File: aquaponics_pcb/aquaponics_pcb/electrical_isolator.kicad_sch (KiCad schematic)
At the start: 0 parts

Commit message: update isolator circuit
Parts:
- added C10: 1uF, Capacitor_SMD:C_0603_1608Metric_Pad1.08x0.95mm_HandSolder, symbol Device:C
- added C11: 100nF, Capacitor_SMD:C_0603_1608Metric_Pad1.08x0.95mm_HandSolder, symbol Device:C
- added C9: 10uF, Capacitor_SMD:C_0603_1608Metric_Pad1.08x0.95mm_HandSolder, symbol Device:C
- added IC3: ADM3260ARSZ, SOP65P780X200-20N, symbol SamacSys_Parts:ADM3260ARSZ
- added Q2: SSM6N35AFE,LF, SOTFL50P160X60-6N, symbol SamacSys_Parts:SSM6N35AFE,LF
- added R11, R12: 1M, Resistor_SMD:R_0603_1608Metric_Pad0.98x0.95mm_HandSolder, symbol Device:R_US
- added R13: 10k, Resistor_SMD:R_0603_1608Metric_Pad0.98x0.95mm_HandSolder, symbol Device:R_US
- added R14, R15, R16: 4.7k, Resistor_SMD:R_0603_1608Metric_Pad0.98x0.95mm_HandSolder, symbol Device:R_US
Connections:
- new net: IC3.13 (VSEL), R13.2, R14.1
- new net: IC3.8 (PDIS), Q2.6 (D), R11.2
- new net Earth_Clean: IC3.11 (GNDISO_1), IC3.14 (GNDISO_2), IC3.16 (GNDISO_3), IC3.20 (GNDISO_4), R14.2
- new net GND: C10.2, C11.2, C9.2, IC3.1 (GNDP_1), IC3.10 (GNDP_4), IC3.5 (GNDP_2), IC3.7 (GNDP_3), Q2.1 (S)
- new net ISO_EN: Q2.2 (G), R12.2
- new net ISO_SCL: IC3.19 (SCL1), R15.2
- new net ISO_SDA: IC3.18 (SDA1), R16.2
- new net SCL: IC3.2 (SCL2)
- new net SDA: IC3.3 (SDA2)
- new net VIN: C10.1, C11.1, C9.1, IC3.4 (VDDP), IC3.9 (VIN), R11.1, R12.1
- new net VISO: IC3.12 (VISO), IC3.17 (VDDISO), R13.1, R15.1, R16.1

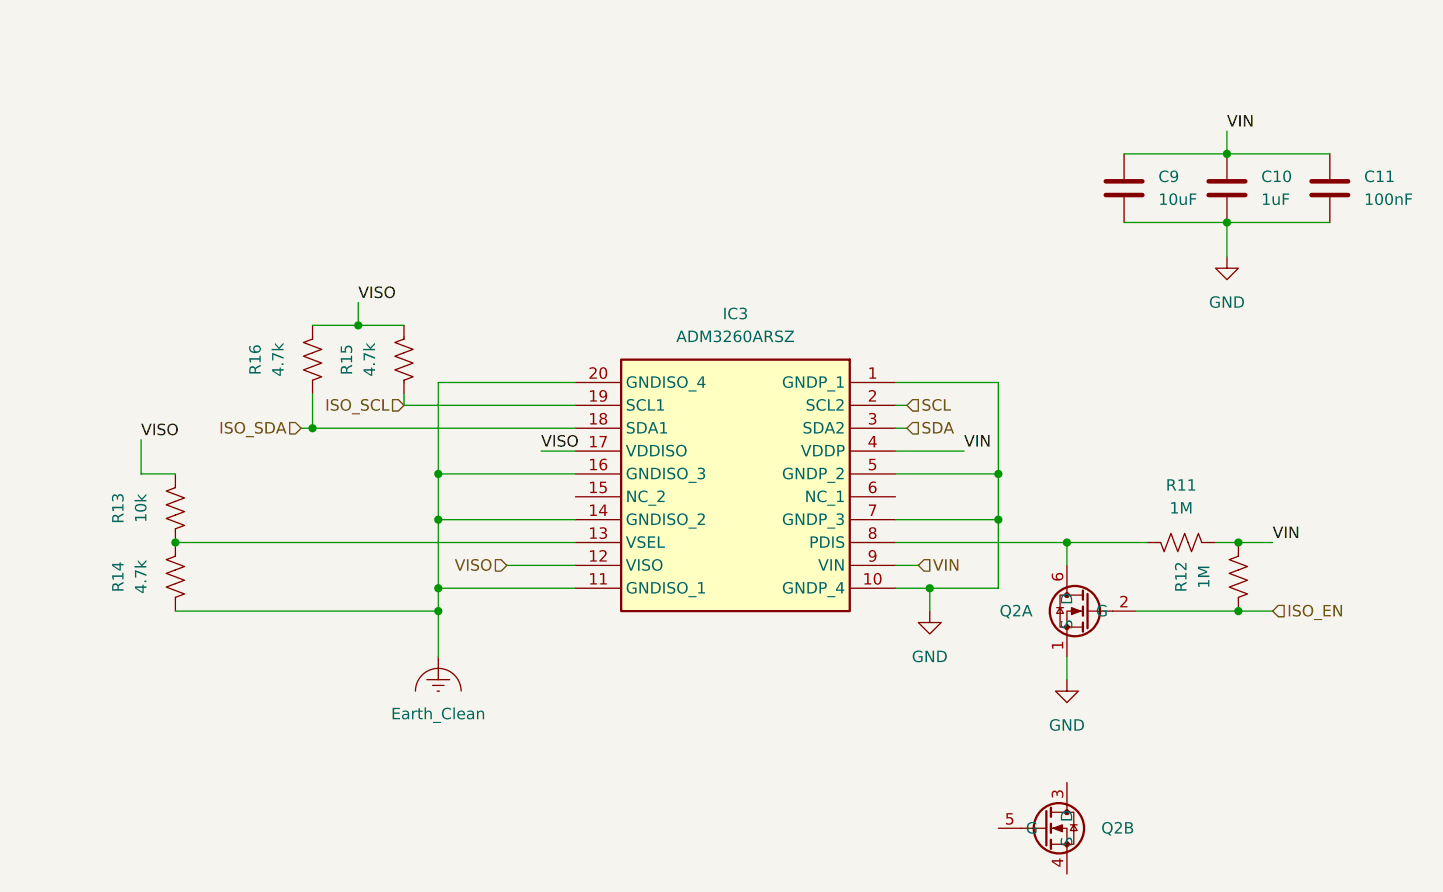
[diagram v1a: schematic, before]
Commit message: begin motor control sch
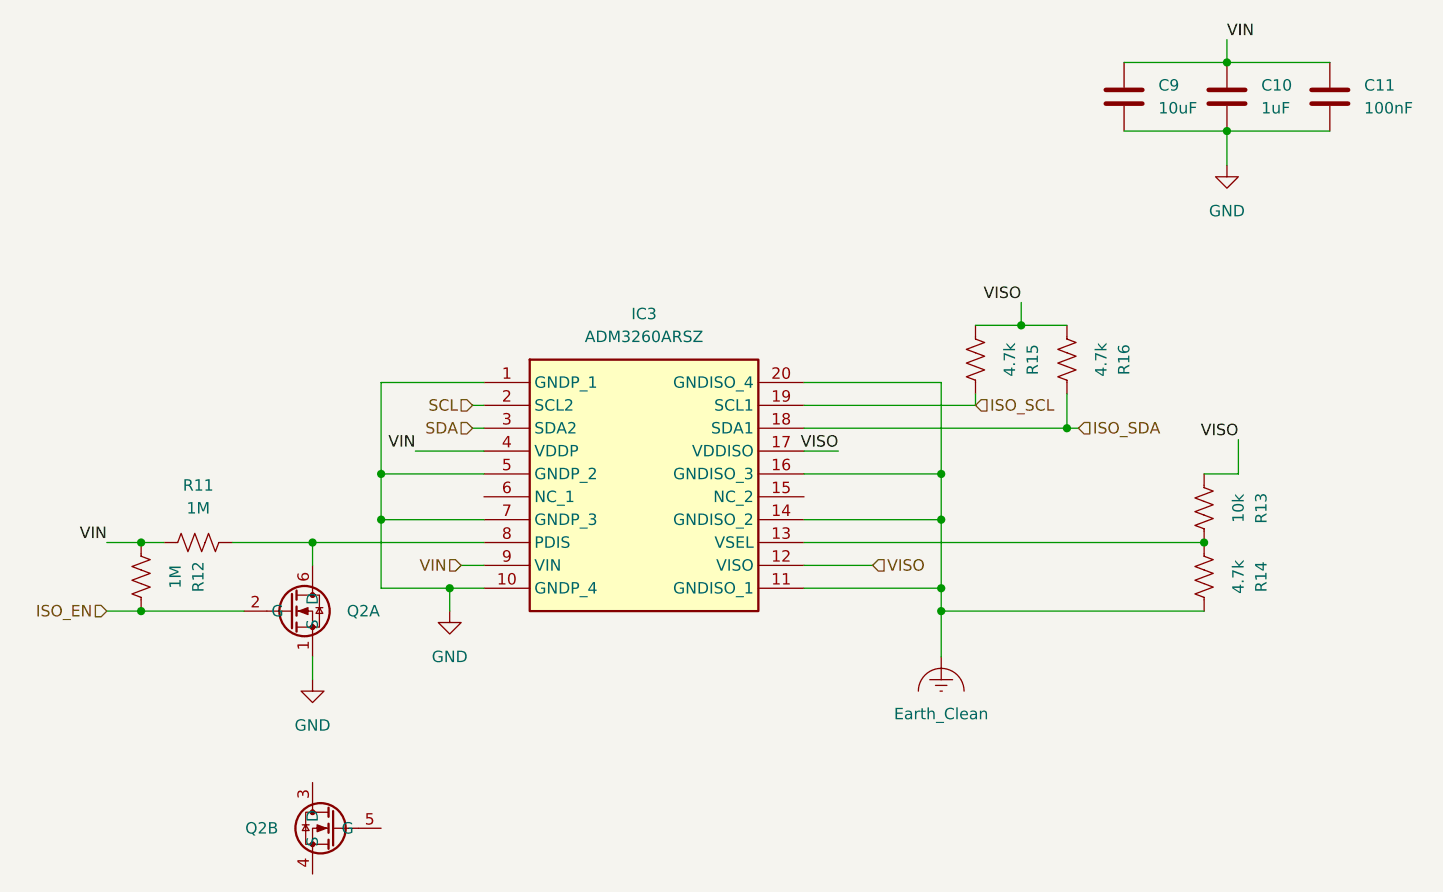
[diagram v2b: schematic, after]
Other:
- moved on the sheet: C10, C11, C9, IC3, Q2A, Q2B, R11, R12, R13, R14, R15, R16

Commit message: add ezo datasheets, update motor schematic and add 2 motors
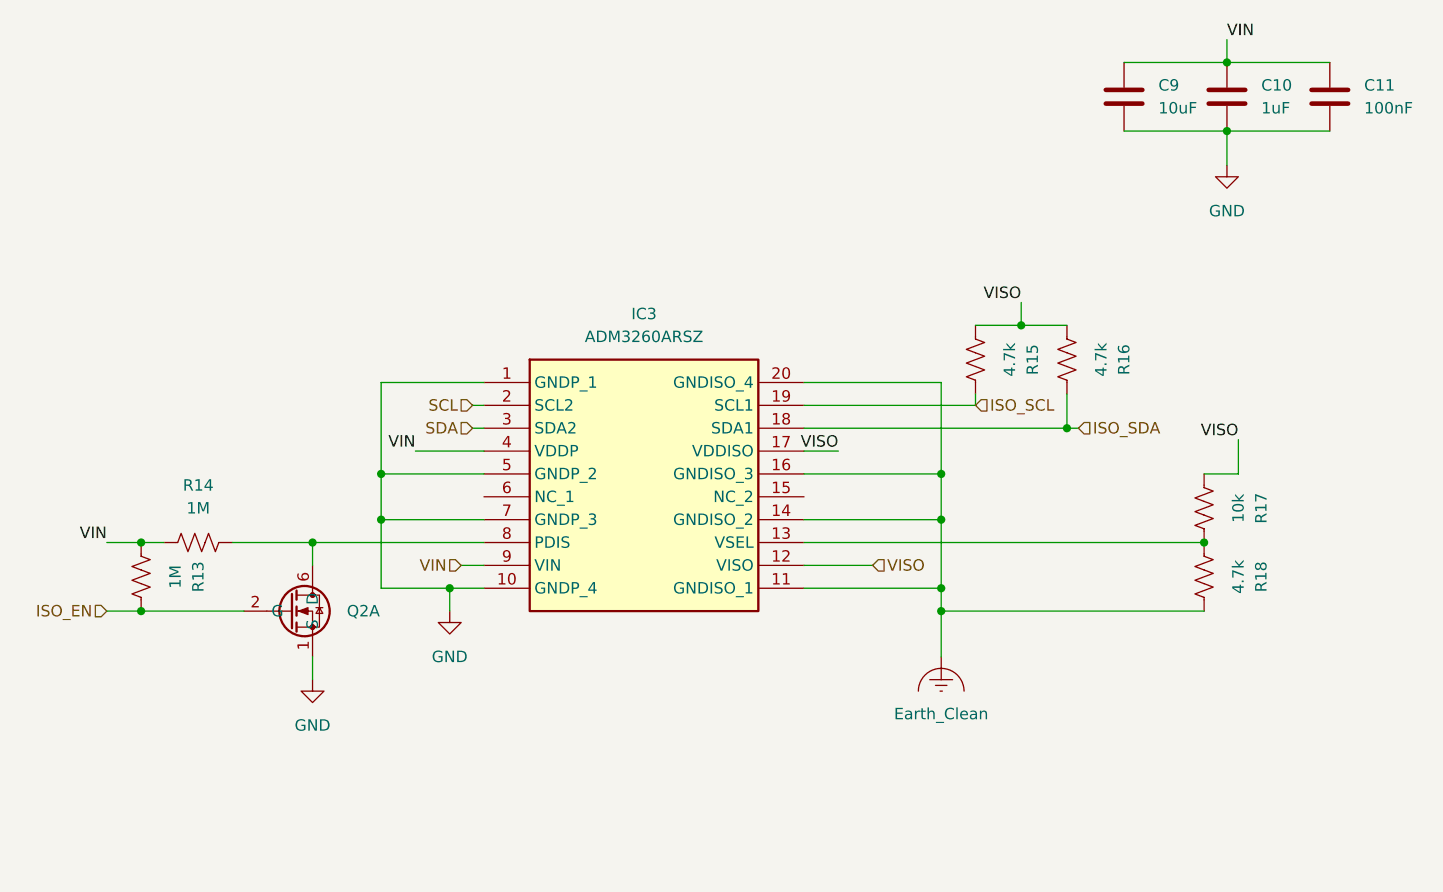
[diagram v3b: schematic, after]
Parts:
- removed unit 2 of Q2
- renumbered R12 to R13, R11 to R14, R13 to R17, R14 to R18
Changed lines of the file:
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@@
 		(dnp no)
 		(fields_autoplaced yes)
-		(property "Reference" "#PWR025"
+		(property "Reference" "#PWR026"
 			(at 102.87 100.33 0)
 			(effects
@@
 			(project "aquaponics_pcb"
 				(path "/c5e5a8d2-0dcc-4520-98a5-511e1dc0d12f/60bf26ba-fc65-4e44-8f3c-45507a542022"
-					(reference "#PWR025")
+					(reference "#PWR026")
 					(unit 1)
 				)
@@
 		(dnp no)
 		(fields_autoplaced yes)
-		(property "Reference" "#PWR022"
+		(property "Reference" "#PWR025"
 			(at 87.63 107.95 0)
 			(effects
@@
 			(project "aquaponics_pcb"
 				(path "/c5e5a8d2-0dcc-4520-98a5-511e1dc0d12f/60bf26ba-fc65-4e44-8f3c-45507a542022"
-					(reference "#PWR022")
+					(reference "#PWR025")
 					(unit 1)
 				)
@@
 		(on_board yes)
 		(dnp no)
-		(property "Reference" "R11"
+		(property "Reference" "R14"
 			(at 74.93 80.01 90)
 			(effects
@@
 			(project "aquaponics_pcb"
 				(path "/c5e5a8d2-0dcc-4520-98a5-511e1dc0d12f/60bf26ba-fc65-4e44-8f3c-45507a542022"
-					(reference "R11")
+					(reference "R14")
 					(unit 1)
 				)
@@
 		(on_board yes)
 		(dnp no)
-		(property "Reference" "R12"
+		(property "Reference" "R13"
 			(at 74.93 90.17 90)
 			(effects
@@
 			(project "aquaponics_pcb"
 				(path "/c5e5a8d2-0dcc-4520-98a5-511e1dc0d12f/60bf26ba-fc65-4e44-8f3c-45507a542022"
-					(reference "R12")
+					(reference "R13")
 					(unit 1)
 				)
@@
 		(dnp no)
 		(fields_autoplaced yes)
-		(property "Reference" "#PWR023"
+		(property "Reference" "#PWR028"
 			(at 189.23 50.8 0)
 			(effects
@@
 			(project "aquaponics_pcb"
 				(path "/c5e5a8d2-0dcc-4520-98a5-511e1dc0d12f/60bf26ba-fc65-4e44-8f3c-45507a542022"
-					(reference "#PWR023")
+					(reference "#PWR028")
 					(unit 1)
 				)
@@
 		(on_board yes)
 		(dnp no)
-		(property "Reference" "R13"
+		(property "Reference" "R17"
 			(at 193.04 82.55 90)
 			(effects
@@
 			(project "aquaponics_pcb"
 				(path "/c5e5a8d2-0dcc-4520-98a5-511e1dc0d12f/60bf26ba-fc65-4e44-8f3c-45507a542022"
-					(reference "R13")
+					(reference "R17")
 					(unit 1)
 				)
@@
 		(dnp no)
 		(fields_autoplaced yes)
-		(property "Reference" "#PWR024"
+		(property "Reference" "#PWR027"
 			(at 157.48 106.68 0)
 			(effects
@@
 			(project "aquaponics_pcb"
 				(path "/c5e5a8d2-0dcc-4520-98a5-511e1dc0d12f/60bf26ba-fc65-4e44-8f3c-45507a542022"
-					(reference "#PWR024")
+					(reference "#PWR027")
 					(unit 1)
 				)
@@
 	)
 	(symbol
-		(lib_id "SamacSys_Parts:SSM6N35AFE,LF")
-		(at 88.9 118.11 0)
-		(mirror y)
-		(unit 2)
-		(exclude_from_sim no)
-		(in_bom yes)
-		(on_board yes)
-		(dnp no)
-		(fields_autoplaced yes)
-		(property "Reference" "Q2"
-			(at 83.82 118.1099 0)
-			(effects
-				(font
-					(size 1.27 1.27)
-				)
-				(justify left)
-			)
-		)
-		(property "Value" "SSM6N35AFE,LF"
-			(at 86.106 113.284 0)
-			(effects
-				(font
-					(size 1.27 1.27)
-				)
-				(justify left top)
-				(hide yes)
-			)
-		)
-		(property "Footprint" "SOTFL50P160X60-6N"
-			(at 54.61 213.03 0)
-			(effects
-				(font
-					(size 1.27 1.27)
-				)
-				(justify left top)
-				(hide yes)
-			)
-		)
-		(property "Datasheet" "http://toshiba.semicon-storage.com/info/docget.jsp?did=55422&prodName=SSM6N35AFE"
-			(at 54.61 313.03 0)
-			(effects
-				(font
-					(size 1.27 1.27)
-				)
-				(justify left top)
-				(hide yes)
-			)
-		)
-		(property "Description" "MOSFET LowON Res MOSFET ID=.25A VDSS=20V"
-			(at 62.992 116.078 0)
-			(effects
-				(font
-					(size 1.27 1.27)
-				)
-				(hide yes)
-			)
-		)
-		(property "Height" "0.6"
-			(at 54.61 513.03 0)
-			(effects
-				(font
-					(size 1.27 1.27)
-				)
-				(justify left top)
-				(hide yes)
-			)
-		)
-		(property "Mouser Part Number" "757-SSM6N35AFELF"
-			(at 54.61 613.03 0)
-			(effects
-				(font
-					(size 1.27 1.27)
-				)
-				(justify left top)
-				(hide yes)
-			)
-		)
-		(property "Mouser Price/Stock" "https://www.mouser.co.uk/ProductDetail/Toshiba/SSM6N35AFELF?qs=BZBei1rCqCAZRZlXQuST4g%3D%3D"
-			(at 54.61 713.03 0)
-			(effects
-				(font
-					(size 1.27 1.27)
-				)
-				(justify left top)
-				(hide yes)
-			)
-		)
-		(property "Manufacturer_Name" "Toshiba"
-			(at 54.61 813.03 0)
-			(effects
-				(font
-					(size 1.27 1.27)
-				)
-				(justify left top)
-				(hide yes)
-			)
-		)
-		(property "Manufacturer_Part_Number" "SSM6N35AFE,LF"
-			(at 54.61 913.03 0)
-			(effects
-				(font
-					(size 1.27 1.27)
-				)
-				(justify left top)
-				(hide yes)
-			)
-		)
-		(pin "6"
-		)
-		(pin "2"
-		)
-		(pin "4"
-		)
-		(pin "5"
-		)
-		(pin "1"
-		)
-		(pin "3"
-		)
-		(instances
-			(project ""
-				(path "/c5e5a8d2-0dcc-4520-98a5-511e1dc0d12f/60bf26ba-fc65-4e44-8f3c-45507a542022"
-					(reference "Q2")
-					(unit 2)
-				)
-			)
-		)
-	)
-	(symbol
 		(lib_id "Device:R_US")
 		(at 186.69 90.17 0)
@@
 		(on_board yes)
 		(dnp no)
-		(property "Reference" "R14"
+		(property "Reference" "R18"
 			(at 193.04 90.17 90)
 			(effects
@@
 			(project "aquaponics_pcb"
 				(path "/c5e5a8d2-0dcc-4520-98a5-511e1dc0d12f/60bf26ba-fc65-4e44-8f3c-45507a542022"
-					(reference "R14")
-					(unit 1)
-				)
+					(reference "R18")
+					(unit 1)
+				)

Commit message: add initial pcb layout
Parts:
- IC3: footprint SOP65P780X200-20N -> SamacSys_Parts:SOP65P780X200-20N
- Q2: footprint SOTFL50P160X60-6N -> SamacSys_Parts:SOTFL50P160X60-6N
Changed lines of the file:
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@@
 			)
 		)
-		(property "Footprint" "SOP65P780X200-20N"
+		(property "Footprint" "SamacSys_Parts:SOP65P780X200-20N"
 			(at 138.43 163.5 0)
 			(effects
@@
 			)
 		)
-		(property "Footprint" "SOTFL50P160X60-6N"
+		(property "Footprint" "SamacSys_Parts:SOTFL50P160X60-6N"
 			(at 120.65 188.9 0)
 			(effects
